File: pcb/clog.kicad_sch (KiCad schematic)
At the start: 24 parts, among them SW1 SW_Push, SW10 SW_Push, SW11 SW_Push, SW12 SW_Push, SW13 SW_Push, SW14 SW_Push, SW15 SW_Push, SW16 SW_Push, SW17 SW_Push, SW18 SW_Push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

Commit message: Rename to the Clog
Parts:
- removed SW21: SW_Push, keyswitches:Kailh_socket_PG1350_optional_reversible, symbol Switch:SW_Push
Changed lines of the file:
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@@
   (no_connect (at 176.53 57.15))
   (no_connect (at 212.09 49.53))
-  (wire (pts (xy 129.54 100.33) (xy 129.54 114.3))
-    (stroke (width 0) (type default) (color 0 0 0 0))
-  )
-  (wire (pts (xy 139.7 100.33) (xy 139.7 114.3))
-    (stroke (width 0) (type default) (color 0 0 0 0))
-  )
   (wire (pts (xy 171.45 116.84) (xy 173.99 116.84))
     (stroke (width 0) (type default) (color 0 0 0 0))
@@
     )
   )
-  (global_label "K16" (shape input) (at 129.54 114.3 270) (fields_autoplaced)
-    (effects (font (size 1.27 1.27)) (justify right))
-    (property "Intersheet References" "${INTERSHEET_REFS}" (id 0) (at 129.4606 120.4021 90)
+  (global_label "K16" (shape input) (at 129.54 100.33 270) (fields_autoplaced)
+    (effects (font (size 1.27 1.27)) (justify right))
+    (property "Intersheet References" "${INTERSHEET_REFS}" (id 0) (at 129.4606 106.4321 90)
       (effects (font (size 1.27 1.27)) (justify right) hide)
     )
@@
     )
   )
-  (global_label "gnd" (shape input) (at 139.7 114.3 270) (fields_autoplaced)
-    (effects (font (size 1.27 1.27)) (justify right))
-    (property "Intersheet References" "${INTERSHEET_REFS}" (id 0) (at 139.6206 120.1602 90)
+  (global_label "gnd" (shape input) (at 139.7 100.33 270) (fields_autoplaced)
+    (effects (font (size 1.27 1.27)) (justify right))
+    (property "Intersheet References" "${INTERSHEET_REFS}" (id 0) (at 139.6206 106.1902 90)
       (effects (font (size 1.27 1.27)) (justify right) hide)
     )
@@
     )
     (property "Datasheet" "~" (id 3) (at 134.62 95.25 0)
-      (effects (font (size 1.27 1.27)) hide)
-    )
-    (pin "1")
-    (pin "2")
-  )
-  (symbol (lib_id "Switch:SW_Push") (at 134.62 114.3 0) (unit 1)
-    (in_bom yes) (on_board yes) (fields_autoplaced)
-    (property "Reference" "SW21" (id 0) (at 134.62 106.68 0))
-    (property "Value" "SW_Push" (id 1) (at 134.62 109.22 0))
-    (property "Footprint" "keyswitches:Kailh_socket_PG1350_optional_reversible" (id 2) (at 134.62 109.22 0)
-      (effects (font (size 1.27 1.27)) hide)
-    )
-    (property "Datasheet" "~" (id 3) (at 134.62 109.22 0)
       (effects (font (size 1.27 1.27)) hide)
     )
@@
       (reference "SW20") (unit 1) (value "SW_SPDT") (footprint "Button_Switch_SMD:SW_SPDT_PCM12")
     )
-    (path "/8f17d345-b64e-472f-8aa0-d96377951d27"
-      (reference "SW21") (unit 1) (value "SW_Push") (footprint "keyswitches:Kailh_socket_PG1350_optional_reversible")
-    )
     (path "/c7a53cab-ad3a-43ee-8585-52abdf784d4b"

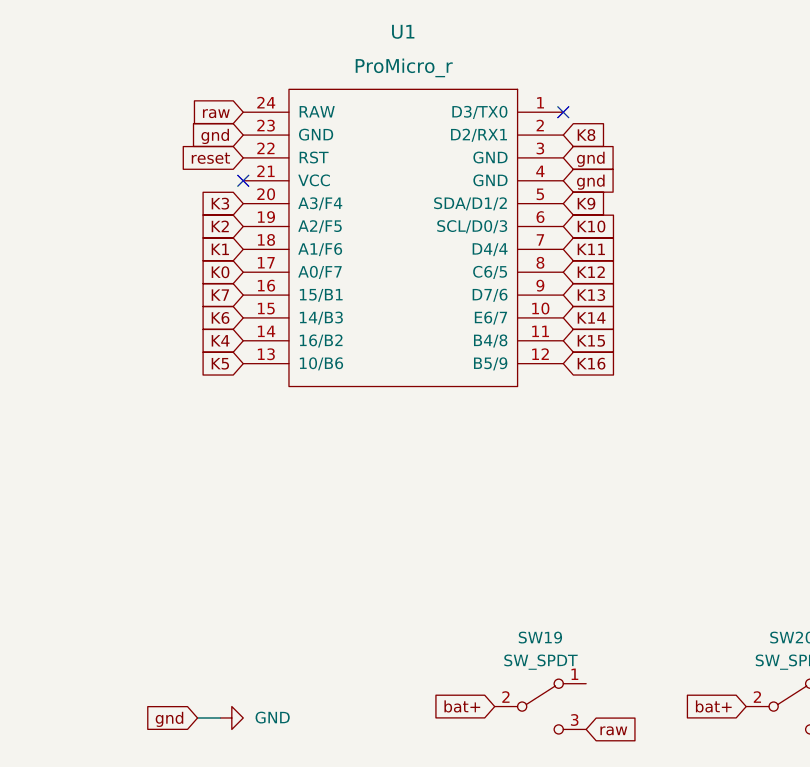
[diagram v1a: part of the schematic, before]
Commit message: add wired split option
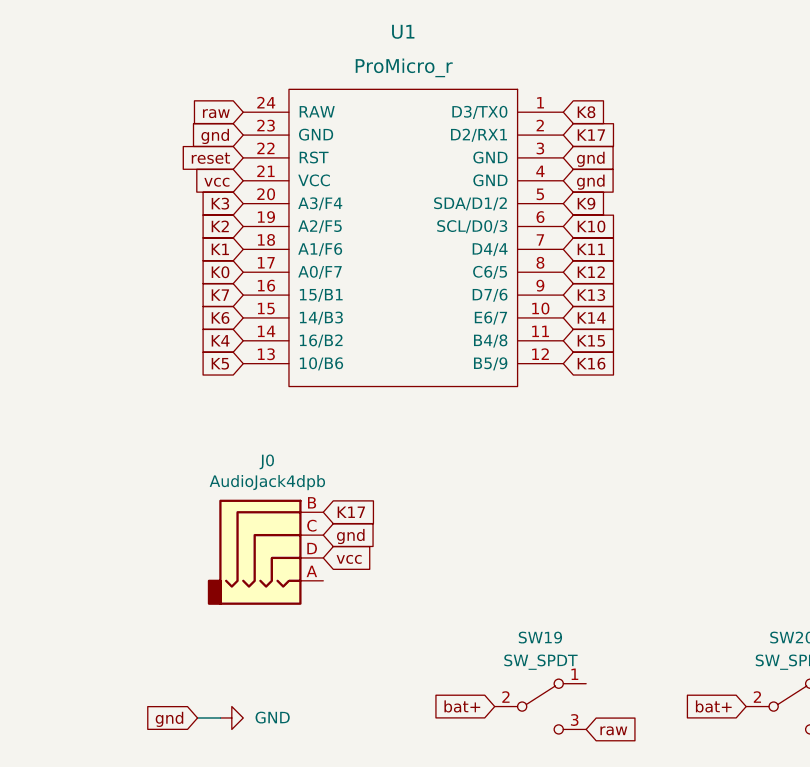
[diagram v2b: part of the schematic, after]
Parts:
- added J0: AudioJack4dpb, kbd:MJ-4PP-9, symbol tokas_bp:AudioJack4dpb
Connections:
- net GND: now also J0.C
- net K8: now also U1.1 (D3/TX0); no longer U1.2 (D2/RX1)
- net vcc: now reaches U1.21 (VCC)
- net vcc: now also J0.D
- new net K17: J0.B, U1.2 (D2/RX1)
- no-connect marks 2 -> 0
